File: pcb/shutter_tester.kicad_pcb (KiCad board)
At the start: 2 copper layers, 53 x 42 mm, 16 parts, among them J1 Conn_01x04, Q1 MMBTA13LT3G, U1 LM393

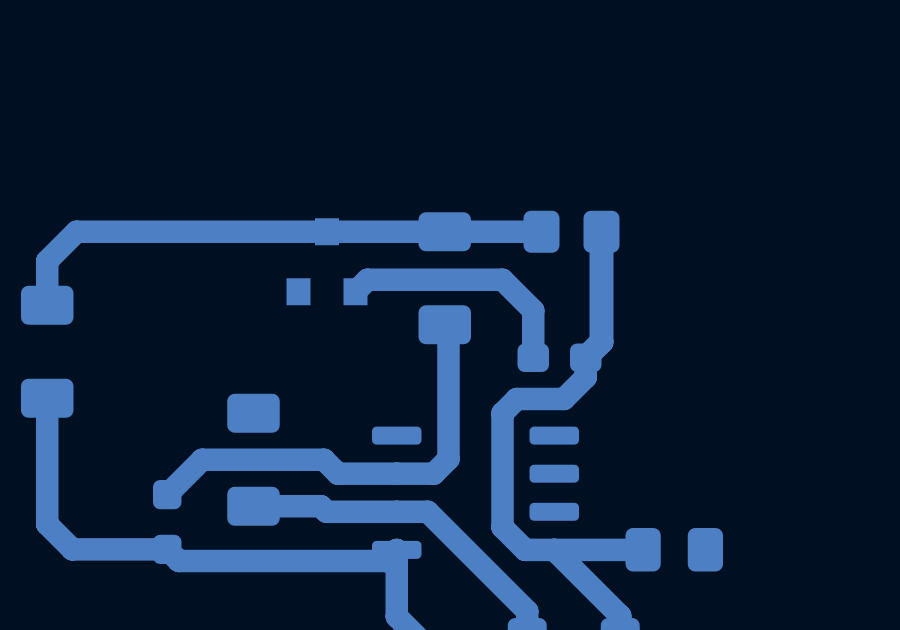
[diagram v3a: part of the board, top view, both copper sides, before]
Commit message: add pulldown resistor to darlington
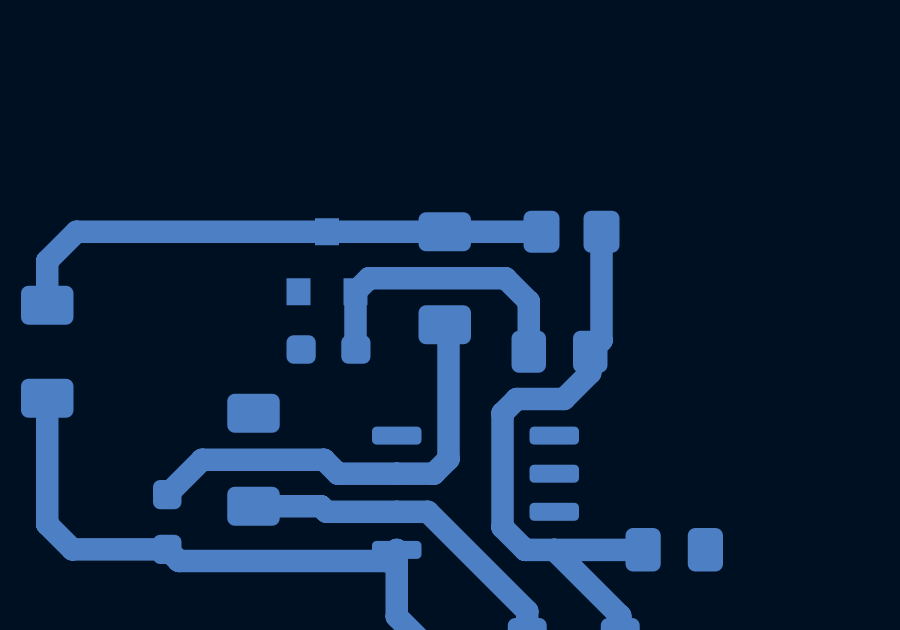
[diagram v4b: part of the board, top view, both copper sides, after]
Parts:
- added R7: 4.7M, Resistor_SMD:R_0603_1608Metric_Pad0.98x0.95mm_HandSolder, B.Cu at (149.4, 121.7)
- D1: footprint LED_SMD:LED_0603_1608Metric_Pad1.05x0.95mm_HandSolder -> LED_SMD:LED_0805_2012Metric_Pad1.15x1.40mm_HandSolder
- R5: value 4.7M -> 102k
- moved D1 0.20 mm to (157.1, 121.8)
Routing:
- net Net-(D1-Pad2): track 8.09 -> 9.89 mm

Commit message: convert to kicad 6
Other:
- net class Default removed

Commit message: getting to rev b layout
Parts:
- removed JP1: Comparitor Bypass, Resistor_SMD:R_1206_3216Metric_Pad1.30x1.75mm_HandSolder
- added C2: 1u, Capacitor_SMD:C_0805_2012Metric_Pad1.18x1.45mm_HandSolder, F.Cu at (152.6, 102.1)
- added D2: LED, LED_SMD:LED_0805_2012Metric_Pad1.15x1.40mm_HandSolder, B.Cu at (151.5, 114.0)
- added Q2: MMBTA13LT3G, Package_TO_SOT_SMD:SOT-23, F.Cu at (151.5, 113.1)
- added R10: 4.7M, Resistor_SMD:R_0603_1608Metric_Pad0.98x0.95mm_HandSolder, F.Cu at (151.5, 116.3)
- added R11: 4.7M, Resistor_SMD:R_0603_1608Metric_Pad0.98x0.95mm_HandSolder, F.Cu at (151.5, 118.3)
- added R12: 4.7M, Resistor_SMD:R_0603_1608Metric_Pad0.98x0.95mm_HandSolder, F.Cu at (151.5, 120.3)
- added R13: 2k, Resistor_SMD:R_0805_2012Metric_Pad1.20x1.40mm_HandSolder, F.Cu at (148.3, 113.1)
- added R14: 10k, Resistor_SMD:R_0603_1608Metric_Pad0.98x0.95mm_HandSolder, F.Cu at (154.5, 113.1)
- added R17: 102k, Resistor_SMD:R_0603_1608Metric_Pad0.98x0.95mm_HandSolder, F.Cu at (156.4, 106.9)
- added R18: 3k, Resistor_SMD:R_0805_2012Metric_Pad1.20x1.40mm_HandSolder, F.Cu at (154.2, 106.4)
- added R8: 4.7M, Resistor_SMD:R_0603_1608Metric_Pad0.98x0.95mm_HandSolder, F.Cu at (141.5, 118.3)
- added R9: 4.7M, Resistor_SMD:R_0603_1608Metric_Pad0.98x0.95mm_HandSolder, F.Cu at (141.5, 120.3)
- C1, Q1, R1, R5, R6, R7, U1: moved to F.Cu
- J1: footprint Connector_PinHeader_2.54mm:PinHeader_1x04_P2.54mm_Horizontal -> Connector_PinHeader_2.54mm:PinHeader_1x04_P2.54mm_Vertical
- R2, R3, R4: footprint Resistor_SMD:R_1206_3216Metric_Pad1.30x1.75mm_HandSolder -> Resistor_SMD:R_0603_1608Metric_Pad0.98x0.95mm_HandSolder; moved to F.Cu
- moved J1 47.6 mm to (142.7, 95.5), turned to 90 degrees
- moved R6 33.8 mm to (138.8, 106.9), turned to 90 degrees
- moved R3 29.6 mm to (141.0, 107.0), turned to -90 degrees
- moved C1 26.9 mm to (155.1, 102.1), turned to 90 degrees
- moved R5 21.9 mm to (136.6, 106.9), turned to -90 degrees
- moved U1 21.1 mm to (146.5, 106.9)
- moved R4 19.2 mm to (152.0, 106.9), turned to 90 degrees
- moved D1 17.4 mm to (141.5, 114.0)
- moved R2 16.0 mm to (138.5, 113.1), turned to -90 degrees
- moved R1 13.6 mm to (144.7, 113.1), turned to -90 degrees
- moved H1 13.6 mm to (124.0, 97.0)
- moved H2 13.6 mm to (124.0, 131.0)
- moved H3 13.6 mm to (169.0, 131.0)
- moved H4 13.6 mm to (169.0, 97.0)
- moved Q1 9.70 mm to (141.5, 113.1)
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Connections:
- J1 pad 1: VCC -> GND
- J1 pad 2: GND -> /OUTPUT_1
- J1 pad 3: /OUTPUT -> /OUTPUT_2
- J1 pad 4: GND -> VCC
- R3 pad 1: Net-(R3-Pad1) -> VCC
- R3 pad 2: VCC -> /Vtrig
- R4 pad 1: GND -> /Vtrig
- R4 pad 2: Net-(R3-Pad1) -> GND
- R5 pad 1: /OUTPUT -> /OUTPUT_1
- R6 pad 1: /OUTPUT -> /OUTPUT_1
- R7 pad 2: GND -> Net-(R7-Pad2)
- U1 pad 1: /OUTPUT -> /OUTPUT_1
- U1 pad 2: Net-(R3-Pad1) -> /Vtrig
- U1 pad 5: GND -> Net-(U1-Pad5)
- U1 pad 6: GND -> /Vtrig
- U1 pad 7: GND -> /OUTPUT_2
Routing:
- net VCC: track 29.9 -> 77.3 mm, vias 0 -> 2
- net /OUTPUT: track 30.2 -> 0.00 mm
- net /OUTPUT_2: track 0.00 -> 21.6 mm
- net /OUTPUT_1: track 0.00 -> 21.1 mm
- net Net-(U1-Pad5): track 0.00 -> 13.3 mm
- net /Vtrig: track 0.00 -> 12.3 mm
- net Net-(R3-Pad1): track 11.7 -> 0.00 mm
- net Net-(Q1-Pad3): track 18.4 -> 7.77 mm
- net GND: track 0.00 -> 9.85 mm, vias 0 -> 10
- net Net-(Q2-Pad3): track 0.00 -> 7.77 mm
- net Net-(D2-Pad2): track 0.00 -> 6.63 mm, vias 0 -> 1
- net Net-(D1-Pad2): track 9.89 -> 6.06 mm, vias 0 -> 1
- net Net-(R8-Pad2): track 0.00 -> 2.00 mm
- net Net-(R7-Pad2): track 0.00 -> 2.00 mm
- net Net-(R11-Pad2): track 0.00 -> 2.00 mm
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- added copper zone on F.Cu, net (none)
- added copper zone on F.Cu, net GND
- added copper zone on F.Cu, net VCC
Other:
- board text added: "Shutter Boundry"

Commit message: rev a layout
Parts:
- added G***: LOGO, PL_logo:logo_height_8mm, F.Cu at (146.5, 127.2)
- added G***: LOGO, PL_logo:logo_height_5mm, B.Cu at (146.5, 128.9)
- moved R13 9.36 mm to (156.3, 118.0), turned to 90 degrees
- moved J1 7.62 mm to (150.3, 95.5), turned to -90 degrees
- moved R14 7.26 mm to (149.1, 118.0), turned to 90 degrees
- moved R7 6.75 mm to (138.9, 122.5), turned to -90 degrees
- moved R10 6.25 mm to (151.7, 122.5), turned to -90 degrees
- moved R12 5.62 mm to (156.7, 122.5), turned to -90 degrees
- moved R2 5.29 mm to (136.4, 118.0), turned to 90 degrees
- moved Q1 5.11 mm to (139.9, 118.0)
- moved R11 5.01 mm to (154.2, 122.5), turned to 90 degrees
- moved Q2 4.97 mm to (152.6, 118.0)
- moved R1 4.97 mm to (143.6, 118.0), turned to 90 degrees
- moved R8 4.25 mm to (141.4, 122.5), turned to 90 degrees
- moved R18 3.67 mm to (157.2, 108.5)
- moved R9 3.33 mm to (143.9, 122.5), turned to -90 degrees
- moved R17 2.45 mm to (154.5, 108.5)
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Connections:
- J1 pad 1: GND -> VCC
- J1 pad 2: /OUTPUT_1 -> /OUTPUT_2
- J1 pad 3: /OUTPUT_2 -> /OUTPUT_1
- J1 pad 4: VCC -> GND
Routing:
- net Net-(Q2-Pad3): track 7.77 -> 0.00 mm
- net Net-(Q1-Pad3): track 7.77 -> 0.00 mm
- net Net-(R2-Pad1): track 14.4 -> 21.7 mm
- net VCC: track 77.3 -> 70.3 mm, vias 2 -> 7
- net Net-(D1-Pad2): track 6.06 -> 10.0 mm
- net Net-(R14-Pad1): track 13.3 -> 16.9 mm
- net GND: track 9.85 -> 12.4 mm, vias 10 -> 8
- net Net-(D2-Pad2): track 6.63 -> 8.78 mm
- net /OUTPUT_2: track 21.6 -> 22.7 mm
- net /Vtrig: track 12.3 -> 11.6 mm
- net Net-(R8-Pad2): track 2.00 -> 2.50 mm
- net Net-(R7-Pad2): track 2.00 -> 2.50 mm
- net Net-(R11-Pad2): track 2.00 -> 2.50 mm
- net Net-(R10-Pad2): track 2.00 -> 2.50 mm
- added copper zone on F.Cu, net Net-(Q1-Pad3)
- added copper zone on F.Cu, net Net-(Q2-Pad3)
- removed copper zone on F.Cu, net (none)
- removed copper zone on F.Cu, net VCC
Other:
- board text added: "10mm"
- board text added: "5V"
- board text added: "A"
- board text added: "B"
- board text added: "GND"
- board text added: "March 2022"
- board text added: "Shutter Timing Sensor"
